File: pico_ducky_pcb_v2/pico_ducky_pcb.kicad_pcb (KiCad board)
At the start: 4 copper layers, 14 x 30 mm, 32 parts, among them J1 USB_A, J3 Conn_ARM_JTAG_SWD_10, SW1 R-667799, SW2 R-667799, U1 AP2127K-3.3, U2 W25Q32JVZP, U3 RP2040, Y1 Crystal_GND24

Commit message: route out most of the pcb
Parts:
- removed D2: NSR0320, Diode_SMD:D_SOD-323
- removed J3: Conn_ARM_JTAG_SWD_10, Connector_PinHeader_1.27mm:PinHeader_2x05_P1.27mm_Vertical
- removed R4: 1k, Resistor_SMD:R_0402_1005Metric
- added JP1: SolderJumper_2_Open, Jumper:SolderJumper-2_P1.3mm_Open_RoundedPad1.0x1.5mm, B.Cu at (81.3, 56.9)
- added R1: 10k, Resistor_SMD:R_0402_1005Metric, F.Cu at (81.5, 61.7)
- C1, C10, C11, C15, C2, C8, C9: moved to B.Cu
- R2: moved to F.Cu
- R6, R7: footprint Resistor_SMD:R_0402_1005Metric -> Resistor_SMD:R_0201_0603Metric
- U1: value AP2127K-3.3 -> MIC5504-3.3YM5; footprint Package_TO_SOT_SMD:SOT-23-5 -> Package_DFN_QFN:UDFN-4-1EP_1x1mm_P0.65mm_EP0.48x0.48mm
- U2: footprint 8-UFDFN:W25Q80DVUXIE TR -> Package_SON:WSON-8-1EP_6x5mm_P1.27mm_EP3.4x4.3mm
- moved D1 13.6 mm to (92.6, 51.8)
- moved C8 11.6 mm to (88.3, 60.5), turned to 180 degrees
- moved C4 10.8 mm to (82.5, 59.4)
- moved SW2 10.7 mm to (92.8, 64.7), turned to -90 degrees
- moved C6 9.61 mm to (82.9, 46.7), turned to 90 degrees
- moved SW1 7.60 mm to (81.2, 64.7)
- moved C2 6.71 mm to (89.5, 55.5), turned to 180 degrees
- moved C3 6.60 mm to (91.7, 55.7), turned to 90 degrees
- moved R5 6.57 mm to (90.9, 65.9), turned to 90 degrees
- moved C11 5.96 mm to (86.3, 55.0), turned to 0 degrees
- moved C15 5.89 mm to (86.3, 54.2), turned to 0 degrees
- moved C9 5.84 mm to (89.3, 54.5), turned to 180 degrees
- moved C7 4.92 mm to (90.1, 53.4), turned to 180 degrees
- moved C14 4.78 mm to (90.3, 52.5), turned to 180 degrees
- moved R2 4.52 mm to (80.9, 54.3), turned to -90 degrees
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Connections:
- SW1 pad B1: /USB_BOOT -> /SAFE_BOOT
- SW1 pad B2: /USB_BOOT -> /SAFE_BOOT
- SW1 pad B3: /USB_BOOT -> /SAFE_BOOT
- Y1 pad 1: Net-(C16-Pad2) -> /X_IN
- Y1 pad 3: /X_IN -> Net-(C16-Pad2)
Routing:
- net /RESET: track 26.2 -> 7.62 mm
- net /USB_BOOT: track 13.7 -> 0.00 mm, vias 1 -> 0
- net GND: track 32.6 -> 20.3 mm, vias 14 -> 21
- net /QSPI_CS: track 7.95 -> 13.6 mm
- net +1V1: track 17.7 -> 12.2 mm, vias 0 -> 2
- net /RGB_DI: track 5.39 -> 0.00 mm
- net /SWCLK: track 5.29 -> 0.00 mm
- net /QSPI_SD0: track 7.83 -> 2.67 mm, vias 2 -> 0
- net /SAFE_BOOT: track 0.00 -> 5.02 mm, vias 0 -> 1
- net /QSPI_SD1: track 4.73 -> 9.55 mm, vias 0 -> 2
- net /USB_-: track 3.22 -> 7.37 mm
- net /SWD: track 3.86 -> 0.00 mm
- net /X_IN: track 9.59 -> 6.20 mm
- net /QSPI_SCLK: track 7.42 -> 4.23 mm, vias 2 -> 0
- net /QSPI_SD3: track 8.12 -> 5.54 mm, vias 2 -> 0
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- removed copper zone on B.Cu, net +3V3
- removed copper zone on F.Cu, net +3V3
- removed copper zone on B.Cu, net +5V
- removed copper zone on F.Cu, net +5V
- removed copper zone on B.Cu, net GND
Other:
- board text removed: "BOOT"
- board text removed: "RP Duck V1"
- board text removed: "USB"

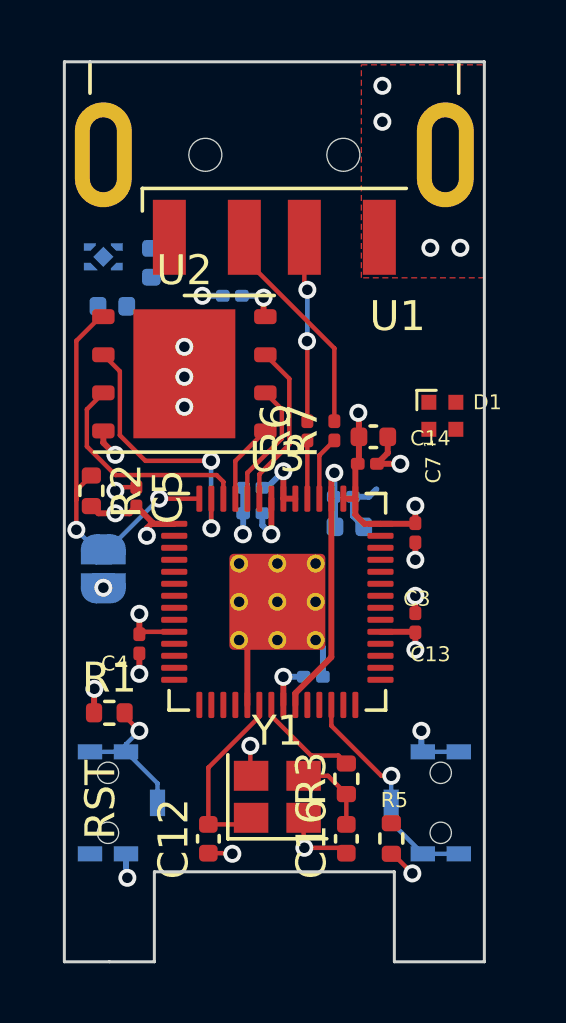
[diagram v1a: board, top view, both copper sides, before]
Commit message: fix issues with mic5504mt compoennt
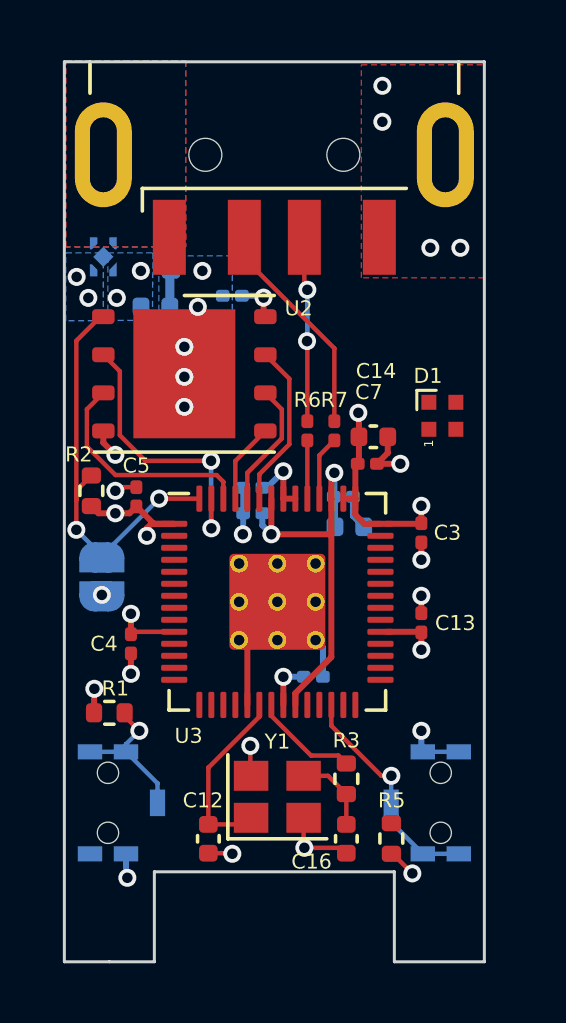
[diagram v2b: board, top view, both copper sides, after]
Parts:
- U1: value MIC5504-3.3YM5 -> MIC5504-3.3YMT
- moved C1 2.57 mm to (83.5, 46.5), turned to 90 degrees
- moved C6 1.48 mm to (83.0, 48.2), turned to 180 degrees
- moved C4 0.28 mm to (82.2, 59.4)
- moved JP1 0.27 mm to (81.2, 57.2)
- moved C13 0.20 mm to (91.9, 58.7)
- moved C3 0.20 mm to (91.9, 55.7)
- turned U1 to 90 degrees
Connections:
- U1 pad 1: +5V -> +3V3
- U1 pad 4: unconnected-(U1-Pad4) -> +5V
- U1 pad 5: +3V3 -> GND
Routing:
- net +1V1: track 12.2 -> 14.2 mm
- net GND: track 20.3 -> 20.0 mm, vias 21 -> 24
- net +3V3: track 22.1 -> 22.2 mm, vias 11 -> 13
- added copper zone on B.Cu, net +3V3
- added copper zone on B.Cu, net +5V
- added copper zone on F.Cu, net +5V
- added copper zone on B.Cu, net GND
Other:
- board text removed: "RST"

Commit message: finish routing neopizel
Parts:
- moved C3 0.15 mm to (92.0, 55.7)
- moved C13 0.15 mm to (92.0, 58.7)
- moved C4 0.07 mm to (82.2, 59.4)
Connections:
- U3 pad 15: /RGB_DI -> unconnected-(U3-Pad15)
- U3 pad 32: /USB_BOOT -> unconnected-(U3-Pad32)
- U3 pad 40: unconnected-(U3-Pad40) -> /RGB_DI
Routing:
- net /RGB_DI: track 0.00 -> 5.43 mm, vias 0 -> 2
- net +3V3: track 22.2 -> 24.7 mm, vias 13 -> 14
- net GND: track 20.0 -> 21.8 mm, vias 24 -> 25
